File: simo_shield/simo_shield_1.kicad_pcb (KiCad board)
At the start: 2 copper layers, 70 x 100 mm, 11 parts, among them J1 Conn_01x02_Female, J2 Conn_01x02_Female, J3 Conn_01x01_Female, U1 elemon_board, U2 modulo_flash_externa, U3 bluepill_board_stm32, U4 modulo_acelerometro

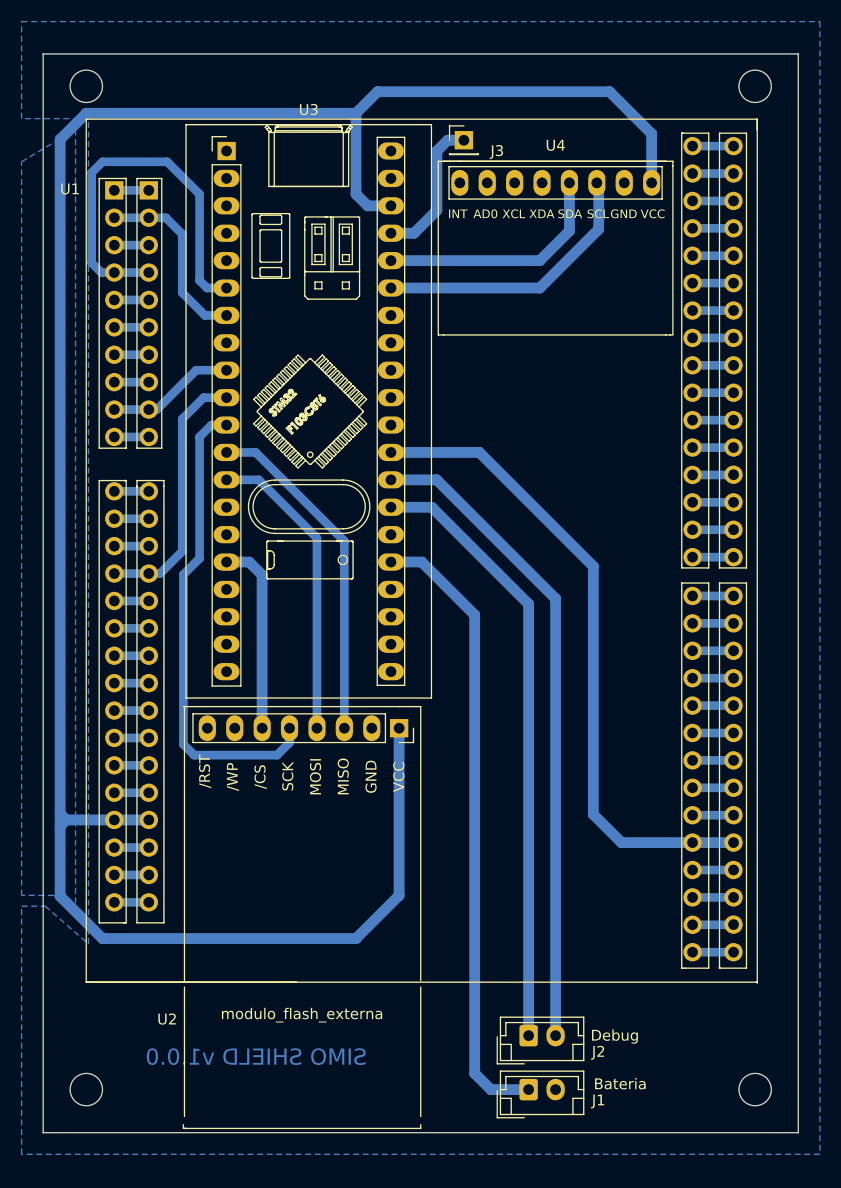
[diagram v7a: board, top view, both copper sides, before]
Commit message: se hizo mas compacto el PCB
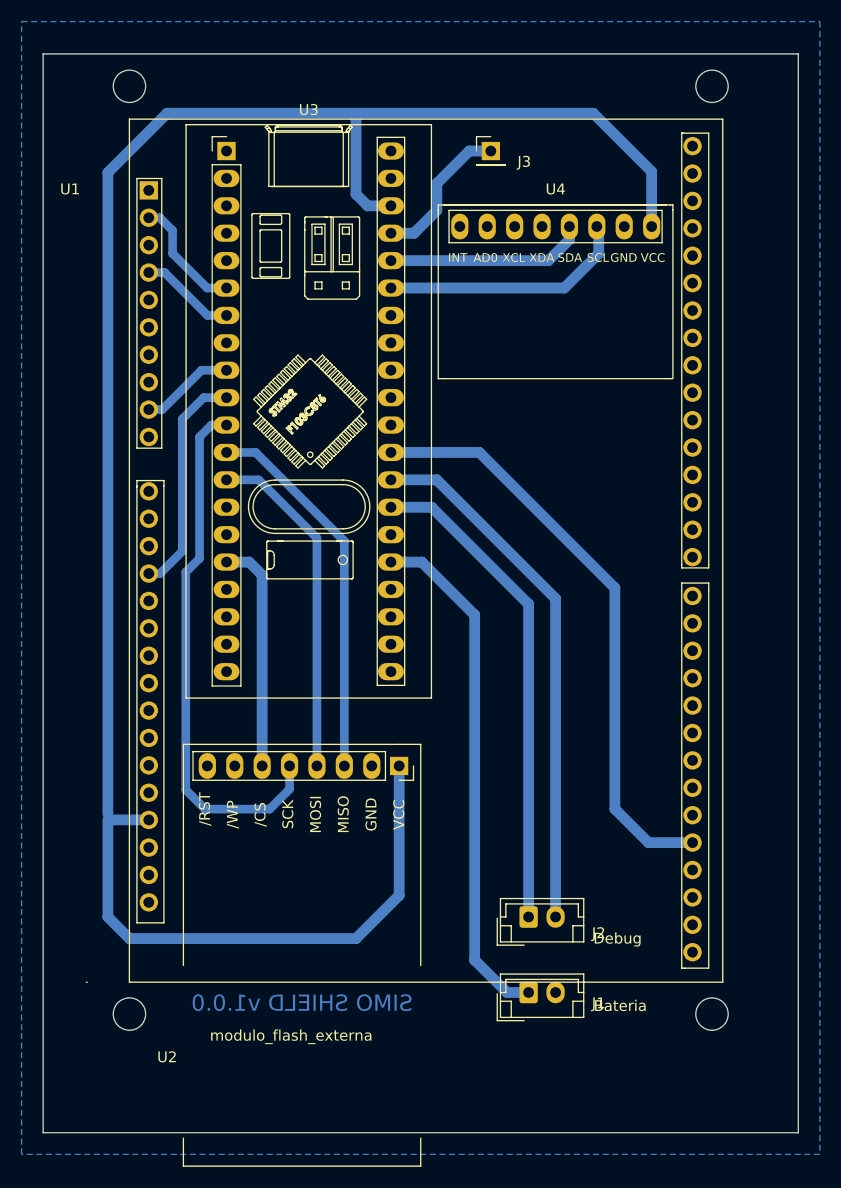
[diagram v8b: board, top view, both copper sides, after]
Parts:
- U1: footprint simo_shield:elemon_board -> simo_shield:elemon_board_compacto
- moved J2 11.0 mm to (156.0, 107.0)
- moved J1 9.00 mm to (156.0, 114.0)
- moved H3 8.06 mm to (173.0, 116.0)
- moved H4 8.06 mm to (119.0, 116.0)
- moved U4 4.05 mm to (149.6, 43.0)
- moved H1 4.00 mm to (119.0, 30.0)
- moved H2 4.00 mm to (173.0, 30.0)
- moved U2 3.50 mm to (144.0, 93.0)
- moved J3 2.69 mm to (152.5, 36.0)
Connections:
- U1 pad 2: Net-(U1-Pad2) -> Net-(U3-Pad6)
- U3 pad 6: Net-(U1-Pad4) -> Net-(U3-Pad6)
- U3 pad 7: Net-(U1-Pad2) -> Net-(U1-Pad4)
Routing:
- net Net-(U1-Pad4): track 36.5 -> 8.85 mm
- net +3.3V: track 203.6 -> 184.3 mm
- net Net-(U1-Pad2): track 17.3 -> 0.00 mm
- net Net-(U3-Pad6): track 0.00 -> 11.2 mm
- net /UART_DEBUG_TX: track 60.3 -> 49.3 mm
- net /UART_DEBUG_RX: track 56.5 -> 45.5 mm
- net Net-(J1-Pad1): track 57.9 -> 48.0 mm
- net Net-(U2-Pad5): track 44.1 -> 49.5 mm
- net /BAT_ENA_PIN: track 60.2 -> 54.9 mm
- net unconnected-(U1-Pad39): track 3.81 -> 0.00 mm
- net unconnected-(U1-Pad55): track 3.81 -> 0.00 mm
- net unconnected-(U1-Pad56): track 3.80 -> 0.00 mm
- net unconnected-(U1-Pad54): track 3.80 -> 0.00 mm
- net unconnected-(U1-Pad53): track 3.80 -> 0.00 mm
- net unconnected-(U1-Pad51): track 3.80 -> 0.00 mm
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- removed copper zone on B.Cu, net +3.3V
